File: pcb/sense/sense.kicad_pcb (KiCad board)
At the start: 2 copper layers, 44 x 42.5 mm, 80 parts, among them J1 PFC24/display, J2 USB_B_Micro, J3 programming, J4 meter, J5 START, J6 SET, J7 RESET, Q1 IRLML0030TR, Q2 BC817, Q3 BC817, Q4 BC817, Q5 BC817, Q6 BC817, Q7 BC817, U1 BME280, U2 STM32G071KxT, U3 TC1185-3.3, U4 MCP73831-2-OT, U5 LIS3MDL, Y1 32k768

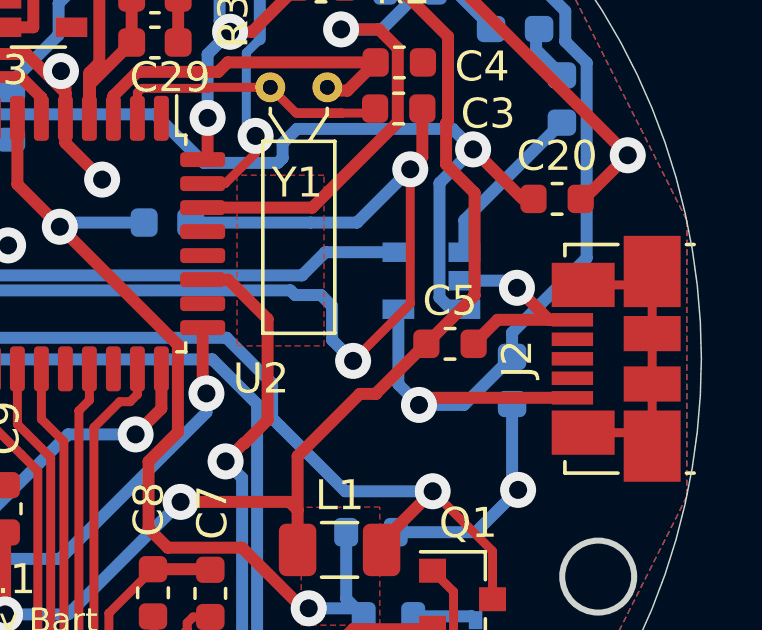
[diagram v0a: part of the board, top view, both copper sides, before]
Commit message: larger C5
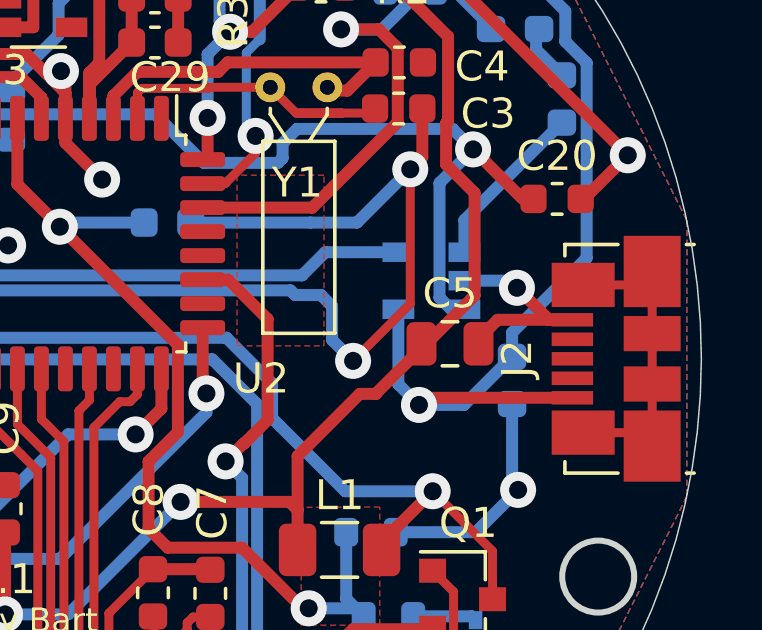
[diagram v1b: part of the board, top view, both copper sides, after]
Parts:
- C5: footprint Capacitor_SMD:C_0603_1608Metric -> Capacitor_SMD:C_0805_2012Metric

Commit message: PCB v1.1
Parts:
- C5: value 475 -> 475 50V
- moved C20 0.99 mm to (176.3, 112.5)
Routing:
- net /VIN: track 58.4 -> 57.6 mm
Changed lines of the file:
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@@
       (effects (font (size 1 1) (thickness 0.15)))
     )
-    (fp_text value "475" (at 0 1.68) (layer "F.Fab")
+    (fp_text value "475 50V" (at 0 1.68) (layer "F.Fab")
       (effects (font (size 1 1) (thickness 0.15)))
     )
@@
     )
     (fp_line (start -3.81 0.06) (end -3.81 -1.71) (layer "F.SilkS") (width 0.12))
-    (fp_line (start 3.81 -1.71) (end 3.81 0.06) (layer "F.SilkS") (width 0.12))
-    (fp_line (start 3.81 -1.71) (end 3.43 -1.71) (layer "F.SilkS") (width 0.12))
-    (fp_line (start -3.81 -1.71) (end -3.43 -1.71) (layer "F.SilkS") (width 0.12))
     (fp_line (start 3.81 2.34) (end 3.81 2.6) (layer "F.SilkS") (width 0.12))
+    (fp_line (start -3.81 -1.71) (end -3.43 -1.71) (layer "F.SilkS") (width 0.12))
+    (fp_line (start 3.81 -1.71) (end 3.43 -1.71) (layer "F.SilkS") (width 0.12))
     (fp_line (start -3.81 2.6) (end -3.81 2.34) (layer "F.SilkS") (width 0.12))
-    (fp_line (start -4.6 3.9) (end -4.6 -2.7) (layer "F.CrtYd") (width 0.05))
-    (fp_line (start 4.6 3.9) (end -4.6 3.9) (layer "F.CrtYd") (width 0.05))
-    (fp_line (start -4.6 -2.7) (end 4.6 -2.7) (layer "F.CrtYd") (width 0.05))
-    (fp_line (start 4.6 -2.7) (end 4.6 3.9) (layer "F.CrtYd") (width 0.05))
-    (fp_line (start 3.75 3.35) (end -3.75 3.35) (layer "F.Fab") (width 0.1))
-    (fp_line (start -3.25 2.65) (end 3.25 2.65) (layer "F.Fab") (width 0.1))
-    (fp_line (start -3.75 3.35) (end -3.75 -1.65) (layer "F.Fab") (width 0.1))
+    (fp_line (start 3.81 -1.71) (end 3.81 0.06) (layer "F.SilkS") (width 0.12))
+    (fp_line (start -4.7 -2.65) (end 4.7 -2.65) (layer "F.CrtYd") (width 0.05))
+    (fp_line (start 4.7 3.85) (end -4.7 3.85) (layer "F.CrtYd") (width 0.05))
+    (fp_line (start 4.7 -2.65) (end 4.7 3.85) (layer "F.CrtYd") (width 0.05))
+    (fp_line (start -4.7 3.85) (end -4.7 -2.65) (layer "F.CrtYd") (width 0.05))
     (fp_line (start 3.75 -1.65) (end 3.75 3.35) (layer "F.Fab") (width 0.1))
+    (fp_line (start -3.75 3.35) (end -3.75 -1.65) (layer "F.Fab") (width 0.1))
     (fp_line (start -3.75 -1.65) (end 3.75 -1.65) (layer "F.Fab") (width 0.1))
-    (pad "1" smd rect locked (at -1.3 -1.46 90) (size 0.45 1.38) (layers "F.Cu" "F.Paste" "F.Mask")
+    (fp_line (start 3.75 3.35) (end -3.75 3.35) (layer "F.Fab") (width 0.1))
+    (fp_line (start -3.25 2.65) (end 3.25 2.65) (layer "F.Fab") (width 0.1))
+    (pad "1" smd rect (at -1.3 -1.46 90) (size 0.45 1.38) (layers "F.Cu" "F.Paste" "F.Mask")
       (net 35 "Net-(C19-Pad1)") (pinfunction "VBUS") (pintype "power_out"))
-    (pad "2" smd rect locked (at -0.65 -1.46 90) (size 0.45 1.38) (layers "F.Cu" "F.Paste" "F.Mask")
+    (pad "2" smd rect (at -0.65 -1.46 90) (size 0.45 1.38) (layers "F.Cu" "F.Paste" "F.Mask")
       (net 24 "unconnected-(J2-Pad2)") (pinfunction "D-") (pintype "passive+no_connect"))
-    (pad "3" smd rect locked (at 0 -1.46 90) (size 0.45 1.38) (layers "F.Cu" "F.Paste" "F.Mask")
+    (pad "3" smd rect (at 0 -1.46 90) (size 0.45 1.38) (layers "F.Cu" "F.Paste" "F.Mask")
       (net 25 "unconnected-(J2-Pad3)") (pinfunction "D+") (pintype "passive+no_connect"))
-    (pad "4" smd rect locked (at 0.65 -1.46 90) (size 0.45 1.38) (layers "F.Cu" "F.Paste" "F.Mask")
+    (pad "4" smd rect (at 0.65 -1.46 90) (size 0.45 1.38) (layers "F.Cu" "F.Paste" "F.Mask")
       (net 26 "unconnected-(J2-Pad4)") (pinfunction "ID") (pintype "passive+no_connect"))
-    (pad "5" smd rect locked (at 1.3 -1.46 90) (size 0.45 1.38) (layers "F.Cu" "F.Paste" "F.Mask")
+    (pad "5" smd rect (at 1.3 -1.46 90) (size 0.45 1.38) (layers "F.Cu" "F.Paste" "F.Mask")
       (net 1 "GND") (pinfunction "GND") (pintype "power_out"))
-    (pad "6" smd rect locked (at -2.91 1.2 90) (size 2.375 1.9) (layers "F.Cu" "F.Paste" "F.Mask")
+    (pad "6" smd rect (at -3.375 1.2 90) (size 1.65 1.3) (layers "F.Cu" "F.Paste" "F.Mask")
       (net 27 "unconnected-(J2-Pad6)") (pinfunction "Shield") (pintype "passive+no_connect"))
-    (pad "6" smd rect locked (at -2.4625 -1.1 90) (size 1.475 2.1) (layers "F.Cu" "F.Paste" "F.Mask")
+    (pad "6" smd rect (at 2.4875 -1.375 90) (size 1.425 1.55) (layers "F.Cu" "F.Paste" "F.Mask")
       (net 27 "unconnected-(J2-Pad6)") (pinfunction "Shield") (pintype "passive+no_connect"))
-    (pad "6" smd rect locked (at 2.4625 -1.1 90) (size 1.475 2.1) (layers "F.Cu" "F.Paste" "F.Mask")
+    (pad "6" smd rect (at 3.375 1.2 90) (size 1.65 1.3) (layers "F.Cu" "F.Paste" "F.Mask")
       (net 27 "unconnected-(J2-Pad6)") (pinfunction "Shield") (pintype "passive+no_connect"))
-    (pad "6" smd rect locked (at -0.84 1.2 90) (size 1.175 1.9) (layers "F.Cu" "F.Paste" "F.Mask")
+    (pad "6" smd rect (at -1.15 1.2 90) (size 1.8 1.9) (layers "F.Cu" "F.Paste" "F.Mask")
       (net 27 "unconnected-(J2-Pad6)") (pinfunction "Shield") (pintype "passive+no_connect"))
-    (pad "6" smd rect locked (at 0.84 1.2 90) (size 1.175 1.9) (layers "F.Cu" "F.Paste" "F.Mask")
+    (pad "6" smd rect (at -2.4875 -1.375 90) (size 1.425 1.55) (layers "F.Cu" "F.Paste" "F.Mask")
       (net 27 "unconnected-(J2-Pad6)") (pinfunction "Shield") (pintype "passive+no_connect"))
-    (pad "6" smd rect locked (at 2.91 1.2 90) (size 2.375 1.9) (layers "F.Cu" "F.Paste" "F.Mask")
+    (pad "6" smd rect (at 1.55 1.2 90) (size 1 1.9) (layers "F.Cu" "F.Paste" "F.Mask")
       (net 27 "unconnected-(J2-Pad6)") (pinfunction "Shield") (pintype "passive+no_connect"))
-    (model "${KISYS3DMOD}/Connector_USB.3dshapes/USB_Micro-B_Molex_47346-0001.wrl"
+    (model "${KICAD6_3DMODEL_DIR}/Connector_USB.3dshapes/USB_Micro-B_Molex_47346-0001.wrl"
       (offset (xyz 0 0 0))
       (scale (xyz 1 1 1))
@@
   )
   (footprint "Capacitor_SMD:C_0603_1608Metric" (layer "F.Cu")
-    (at 176.7 113.45)
+    (at 176.33 112.53)
     (descr "Capacitor SMD 0603 (1608 Metric), square (rectangular) end terminal, IPC_7351 nominal, (Body size source: http://www.tortai-tech.com/upload/download/2011102023233369053.pdf), generated with kicad-footprint-generator")
     (tags "capacitor")
@@
     (property "Sheetname" "")
     (attr smd)
-    (fp_text reference "C20" (at 0 -1.43) (layer "F.SilkS")
+    (fp_text reference "C20" (at 0.97 -1.44) (layer "F.SilkS")
       (effects (font (size 1 1) (thickness 0.15)))
     )
@@
   (segment (start 161.76 127.2625) (end 163.23 125.7925) (width 0.3) (layer "F.Cu") (net 1))
   (segment (start 175.3616 116.41328) (end 176.42832 117.48) (width 0.4) (layer "F.Cu") (net 1))
+  (segment (start 177.6525 111.995) (end 177.1175 112.53) (width 0.4) (layer "F.Cu") (net 1))
   (segment (start 169.995 104.505) (end 171.565 104.505) (width 0.4) (layer "F.Cu") (net 1))
   (segment (start 151.48222 117.46972) (end 151.6125 117.6) (width 0.4) (layer "F.Cu") (net 1))
@@
   (segment (start 176.42832 117.48) (end 177.21 117.48) (width 0.4) (layer "F.Cu") (net 1))
   (segment (start 171.8056 116.9444) (end 169.9 118.85) (width 0.3) (layer "F.Cu") (net 1))
+  (segment (start 179.055 111.995) (end 177.6525 111.995) (width 0.4) (layer "F.Cu") (net 1))
   (segment (start 160.31 110.765) (end 160.31 109.915) (width 0.4) (layer "F.Cu") (net 1))
   (segment (start 172.2075 112.06168) (end 171.8056 112.46358) (width 0.4) (layer "F.Cu") (net 1))
@@
   (segment (start 156.389999 101.614001) (end 156.389999 100.909999) (width 0.4) (layer "F.Cu") (net 1))
   (segment (start 163.41 135.6) (end 169.22 135.6) (width 0.3) (layer "F.Cu") (net 1))
-  (segment (start 177.6 113.45) (end 179.055 111.995) (width 0.4) (layer "F.Cu") (net 1))
   (segment (start 142.6 112.675) (end 146 112.675) (width 0.4) (layer "F.Cu") (net 1))
   (segment (start 156.4386 133.17982) (end 157.26 132.35842) (width 0.3) (layer "F.Cu") (net 1))
@@
   (segment (start 147.629999 116.500001) (end 146.15 117.98) (width 0.4) (layer "B.Cu") (net 1))
   (segment (start 146.54 123.07) (end 146.54 123.22) (width 0.4) (layer "B.Cu") (net 1))
-  (segment (start 175.55 113.45) (end 175.9125 113.45) (width 0.25) (layer "F.Cu") (net 2))
   (segment (start 154.54 104.032) (end 154.54 104.3125) (width 0.4) (layer "F.Cu") (net 2))
   (segment (start 156.4895 106.1465) (end 156.806 105.83) (width 0.4) (layer "F.Cu") (net 2))
   (segment (start 155.448 106.1465) (end 155.448 105.609) (width 0.4) (layer "F.Cu") (net 2))
+  (segment (start 174.8125 111.8) (end 175.5425 112.53) (width 0.4) (layer "F.Cu") (net 2))
   (segment (start 154.54 102.04) (end 154.54 104.032) (width 0.4) (layer "F.Cu") (net 2))
+  (segment (start 173.9 111.8) (end 174.8125 111.8) (width 0.4) (layer "F.Cu") (net 2))
   (segment (start 159.24 105.83) (end 158.31 105.83) (width 0.4) (layer "F.Cu") (net 2))
   (segment (start 155.448 105.609) (end 154.54 104.701) (width 0.4) (layer "F.Cu") (net 2))
   (segment (start 152.586 102.04) (end 152.146 101.6) (width 0.4) (layer "F.Cu") (net 2))
   (segment (start 156.806 105.83) (end 158.31 105.83) (width 0.4) (layer "F.Cu") (net 2))
-  (segment (start 173.9 111.8) (end 175.55 113.45) (width 0.4) (layer "F.Cu") (net 2))
   (segment (start 159.240001 107.729999) (end 159.24 105.83) (width 0.4) (layer "F.Cu") (net 2))
   (segment (start 154.54 104.701) (end 154.54 104.032) (width 0.4) (layer "F.Cu") (net 2))
